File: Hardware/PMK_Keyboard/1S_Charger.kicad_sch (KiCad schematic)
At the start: 12 parts, among them U301 BQ24075RGTR

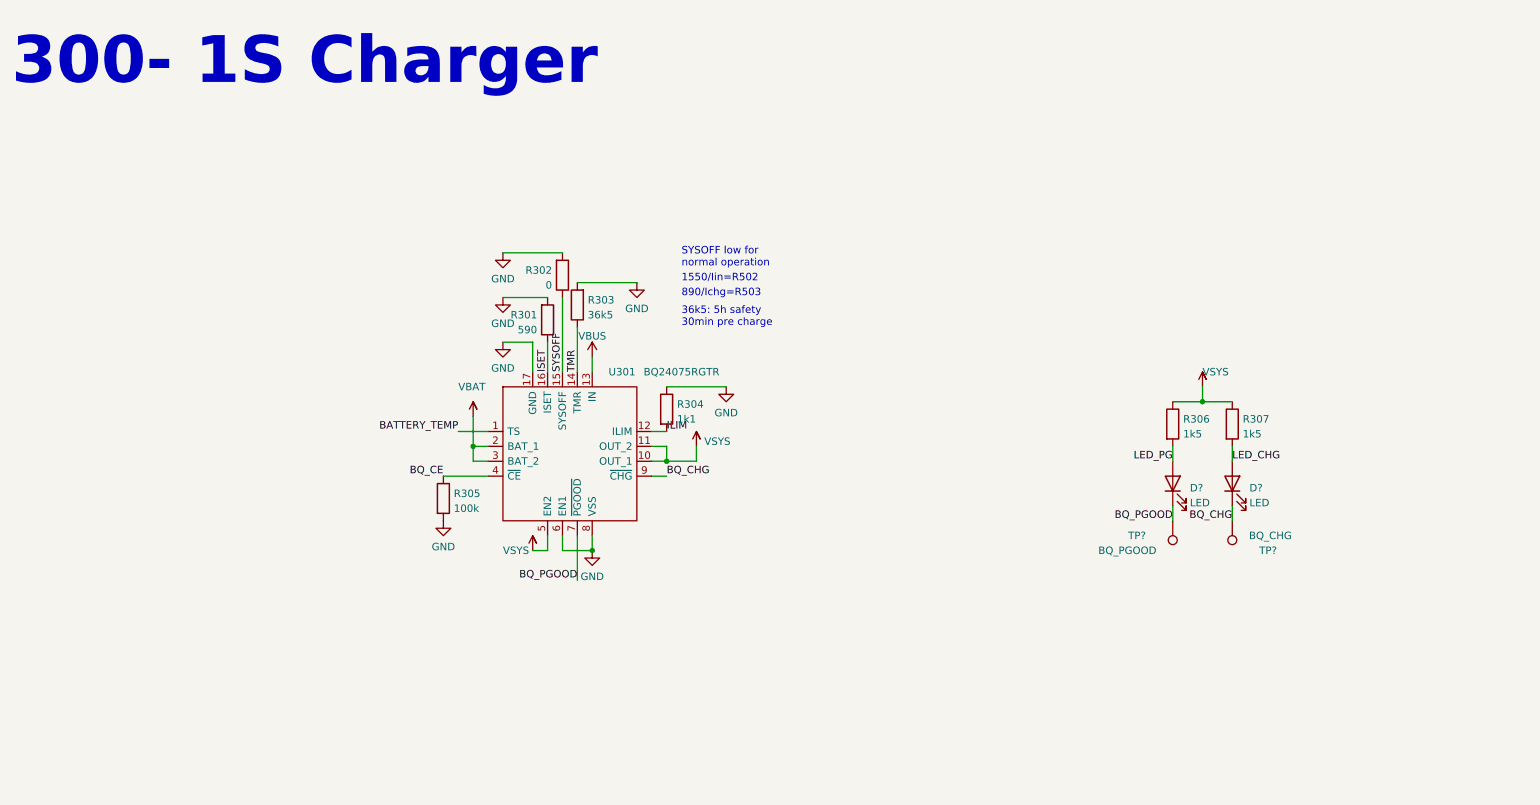
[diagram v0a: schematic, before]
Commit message: Worked on hierachic page again
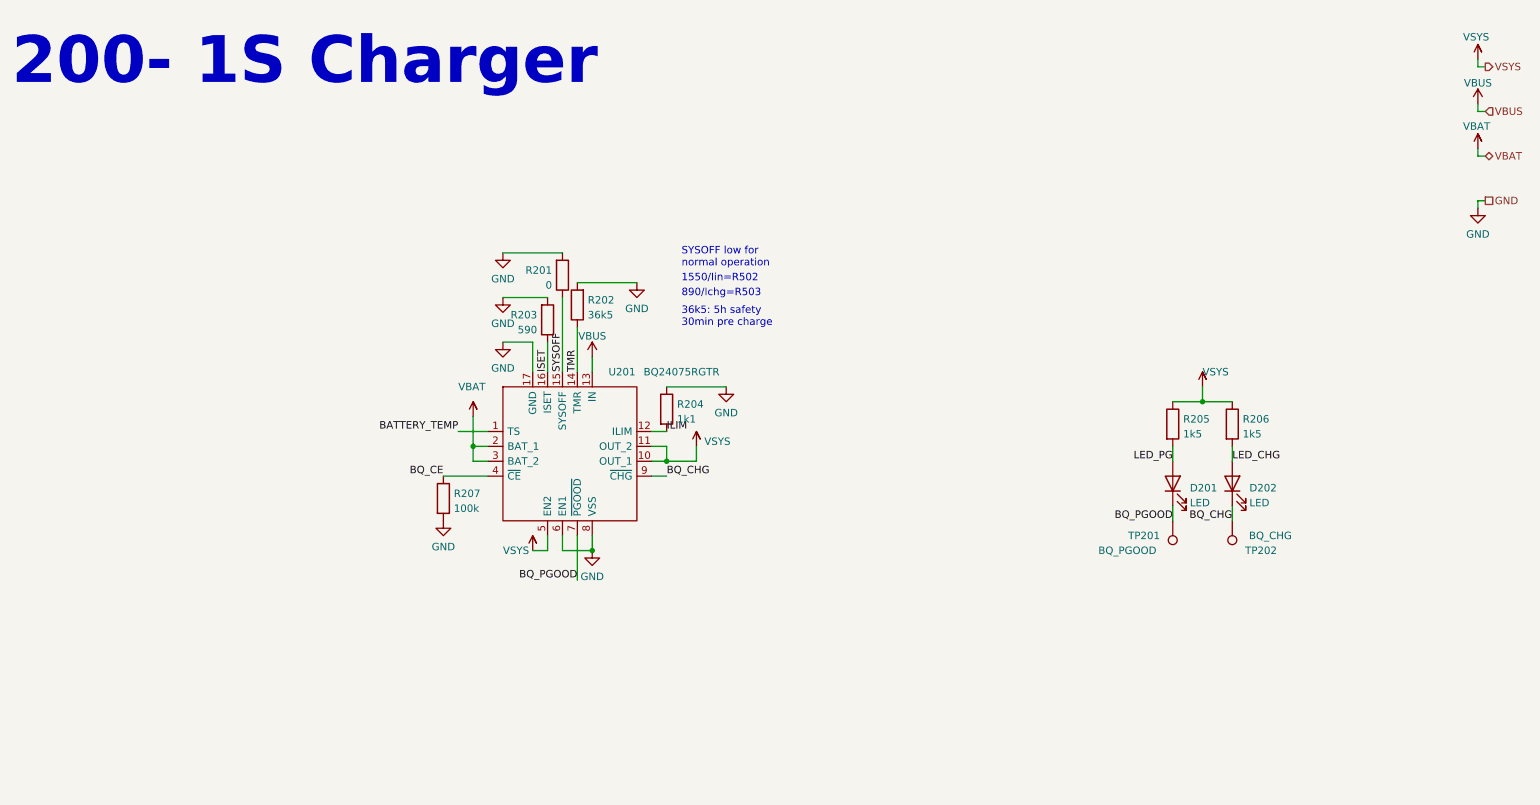
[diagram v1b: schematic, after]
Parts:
- gave numbers to parts that had none: 4
- renumbered R302 to R201, R303 to R202, R301 to R203, R304 to R204, R306 to R205, R307 to R206, R305 to R207, U301 to U201
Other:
- note added: "200- 1S Charger"
- note removed: "300- 1S Charger"

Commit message: Again on hierachic sheet
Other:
- company: (none) -> PumaCorp
- title: (none) -> PMK_Keyboard
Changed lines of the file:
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@@
 (kicad_sch (version 20211123) (generator eeschema)
   (paper "A4")
+  (title_block
+    (title "PMK_Keyboard")
+    (date "2023-02-06")
+    (rev "HW00")
+    (company "PumaCorp")
+    (comment 1 "Design by: NdG")
+  )
   (junction (at 218.44 81.28) (diameter 0) (color 0 0 0 0)
   )

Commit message: Routing is finally updated
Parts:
- R201: footprint Capacitor_SMD:C_0402_1005Metric -> Resistor_SMD:R_0402_1005Metric
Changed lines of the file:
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@@
       (effects (font (size 1.27 1.27)) (justify right))
     )
-    (property "Footprint" "Capacitor_SMD:C_0402_1005Metric" (id 2) (at 107.442 59.69 90)
+    (property "Footprint" "Resistor_SMD:R_0402_1005Metric" (id 2) (at 107.442 59.69 90)
       (effects (font (size 1.27 1.27)) hide)
     )

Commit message: Routing is almost done
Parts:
- removed TP201: BQ_PGOOD, TestPoint:TestPoint_Pad_D1.0mm, symbol Connector:TestPoint
- removed TP202: BQ_CHG, TestPoint:TestPoint_Pad_D1.0mm, symbol Connector:TestPoint
- added C201, C203: 4u7, Capacitor_SMD:C_0603_1608Metric, symbol Component lib:C
- added C202: 1u, Capacitor_SMD:C_0603_1608Metric, symbol Component lib:C
- D201, D202: footprint Capacitor_SMD:C_0402_1005Metric -> Component_lib:LED_0402_1005Metric_DUALSIDE
- R202, R203, R204, R205, R206, R207: footprint Capacitor_SMD:C_0402_1005Metric -> Resistor_SMD:R_0402_1005Metric
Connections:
- net GND: now also C201.2, C202.2, C203.2
- net VBAT: now also U201.2 (BAT_1), U201.3 (BAT_2), C201.1
- net VBUS: now also C202.1
- net VSYS: now also R205.1, R206.1, U201.10 (OUT_1), U201.11 (OUT_2), U201.5 (EN2), C203.1
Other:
- note added: "1u to 10u"
- note added: "4u7 to 47u"

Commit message: quick update
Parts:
- added TP201: TestPoint, TestPoint:TestPoint_Pad_D1.0mm, symbol Connector:TestPoint
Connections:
- net BATTERY_TEMP: now also TP201.1
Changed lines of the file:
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@@
     (stroke (width 0) (type default))
   )
-  (wire (pts (xy 91.44 86.36) (xy 96.52 86.36))
+  (wire (pts (xy 76.2 86.36) (xy 96.52 86.36))
     (stroke (width 0) (type default))
   )
@@
         )
       )
+    )
+  )
+  (symbol (lib_id "Connector:TestPoint") (at 76.2 86.36 0) (unit 1)
+    (in_bom yes) (on_board yes) (dnp no)
+    (property "Reference" "TP201" (at 66.04 81.28 0)
+      (effects (font (size 1.27 1.27)) (justify left))
+    )
+    (property "Value" "TestPoint" (at 66.04 83.82 0)
+      (effects (font (size 1.27 1.27)) (justify left))
+    )
+    (property "Footprint" "TestPoint:TestPoint_Pad_D1.0mm" (at 81.28 86.36 0)
+      (effects (font (size 1.27 1.27)) hide)
+    )
+    (property "Datasheet" "~" (at 81.28 86.36 0)
+      (effects (font (size 1.27 1.27)) hide)
+    )
+    (pin "1")
+    (instances
+      (project "PMK_Keyboard"
+        (path "/c3b08055-08a5-4979-9bf8-f36ab0917722/2d6b4425-2527-49bd-b090-a8cc21f6a212"
+          (reference "TP201") (unit 1)
+        )
+      )
